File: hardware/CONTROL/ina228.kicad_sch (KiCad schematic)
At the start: 5 parts, among them U4 INA228

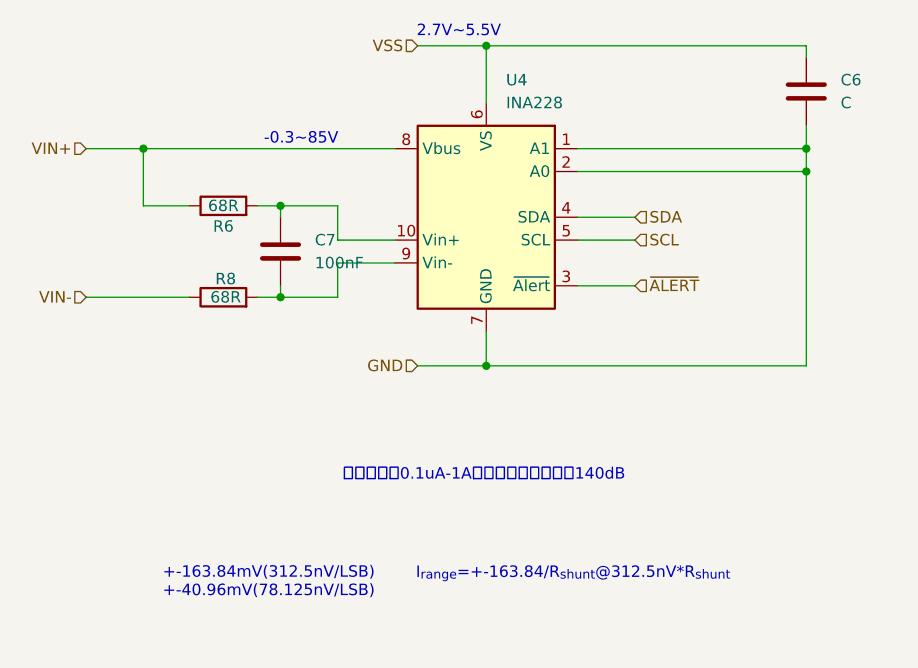
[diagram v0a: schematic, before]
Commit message: PD24 控制部分的PCB设计完成
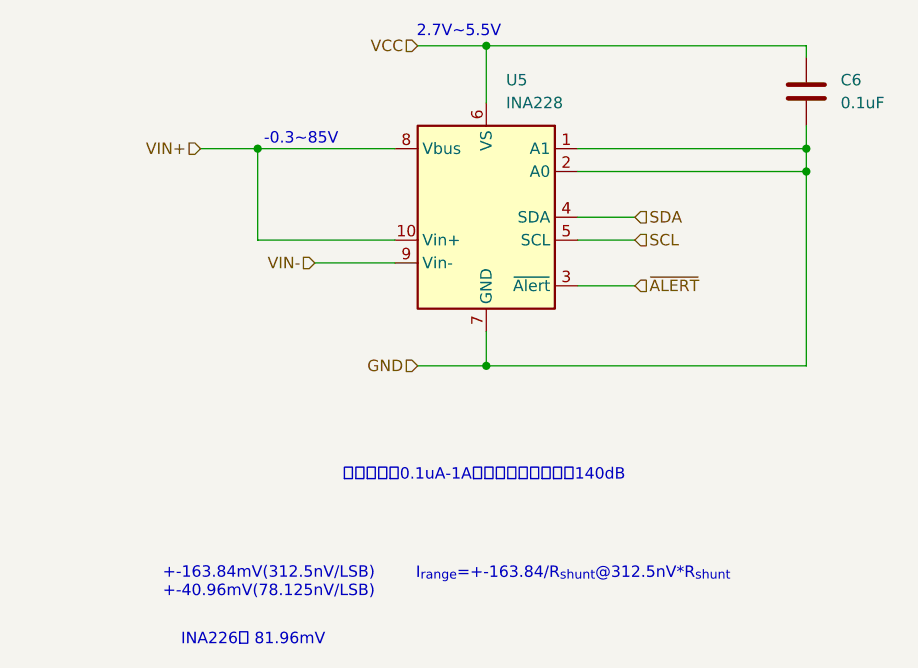
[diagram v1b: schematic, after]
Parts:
- removed C7: 100nF, Capacitor_SMD:C_0402_1005Metric, symbol Device:C
- removed R6, R8: 68R, Resistor_SMD:R_0402_1005Metric, symbol Device:R
- C6: value C -> 0.1uF
- renumbered U4 to U5
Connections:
- net VIN+: now also U5.10 (Vin+)
- net VIN-: now also U5.9 (Vin-)
- net VSS renamed VCC
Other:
- note added: "INA226为 81.96mV"
